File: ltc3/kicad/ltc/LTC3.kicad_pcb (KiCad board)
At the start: 4 copper layers, 175 x 150 mm, 158 parts, among them IC601 TLP3542, IC701 TLP3542, IC702 TLP3542, IC703 TLP3542, IC704 TLP3542, IC801 TLP3542, IC802 TLP3542, IC803 TLP3542, IC804 TLP3542, J601 RJ45, K601 RELAY_1C, K602 RELAY_1C, P401 43045-1000, P501 BeagleBone_Black_Expansion_He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, P502 BeagleBone_Black_Expansion_He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, P601 BATT-IN, P603 UMBILICAL, P605 43045-0200, P606 S4B-PH-K, P607 43045-0200, P608 43025-0200, P701 43045-1000, P703 43045-0800, P705 43045-0800, P801 43045-1000, P803 43045-0800, P805 43045-0800, Q401 BSS138, Q402 BSS138, Q403 BSS138, Q601 PMV45EN, Q602 PMV45EN, Q603 ZVN4525E6, Q604 ZVN4525E6, Q605 ZVN4525E6, Q701 PMV45EN, Q702 PMV45EN, Q703 PMV45EN, Q704 PMV45EN, Q801 PMV45EN, Q802 PMV45EN, Q803 PMV45EN, Q804 PMV45EN, U401 PTN78020W, U402 LTC2991, U403 PTN78020H, U404 PTN78020H, U501 24C256, U601 CD74HC14, U602 SN65220DBV, U603 741G08

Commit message: LTC3: Continued on ignition board layout
Got a solid chunk of work done on the ignition board layout.
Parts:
- moved P606 288.9 mm to (58.0, 113.0), turned to 270 degrees
- moved Q603 287.2 mm to (68.6, 113.7)
- moved R617 284.1 mm to (68.6, 118.2), turned to 270 degrees
- moved Q604 280.3 mm to (77.5, 113.7)
- moved Q605 273.8 mm to (86.3, 113.7)
- moved C602 273.4 mm to (84.1, 83.3), turned to 270 degrees
- moved K601 271.9 mm to (78.8, 97.8), turned to 180 degrees
- moved R609 270.5 mm to (93.5, 73.9), turned to 180 degrees
- moved R618 248.7 mm to (77.5, 118.2), turned to 270 degrees
- moved R619 245.9 mm to (86.3, 118.2), turned to 270 degrees
- moved K602 231.8 mm to (105.2, 95.0)
- moved P605 227.8 mm to (95.3, 114.0), turned to 0 degrees
- moved R610 220.6 mm to (99.9, 73.2), turned to 270 degrees
- moved D603 220.5 mm to (104.2, 68.7), turned to 180 degrees
- moved D605 217.7 mm to (121.5, 105.6), turned to 270 degrees
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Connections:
- net /BeagleBone Black Cape/12V_ENn renamed /12V_ENn
- net /BeagleBone Black Cape/19V_ENn renamed /19V_ENn
- net /BeagleBone Black Cape/BQ_EEPROM renamed /IGN_RTL
- net /BeagleBone Black Cape/EXT_PWR_EN_4 renamed /UMB_CONn
- net /BeagleBone Black Cape/EXT_TRG_EN_1 renamed /EXT_TRG_EN_1
- net /BeagleBone Black Cape/EXT_TRG_EN_2 renamed /EXT_TRG_EN_2
- net /BeagleBone Black Cape/EXT_TRG_EN_3 renamed /EXT_TRG_EN_3
- net /BeagleBone Black Cape/EXT_TRG_EN_4 renamed /EXT_TRG_EN_4
- net /BeagleBone Black Cape/I2C_CLOCK renamed /I2C_CLOCK
- net /BeagleBone Black Cape/I2C_DATA renamed /I2C_DATA
- net /BeagleBone Black Cape/ROCKET_READYn renamed /ROCKET_READYn
- net /External Device Power/EXT_PWR_EN_1 renamed /GPIO_EXT_PWR_1
- net /External Device Power/EXT_PWR_EN_2 renamed /GPIO_EXT_PWR_2
- net /External Device Power/EXT_PWR_EN_3 renamed /GPIO_EXT_PWR_3
- net /External Device Power/EXT_PWR_EN_4 renamed /GPIO_EXT_PWR_4
- K601 pad 1: (no net) -> /Rocket Umbilical & Ignition Control/IGN_BATT_P
- K601 pad 2: (no net) -> +5V
- K601 pad 3: (no net) -> Net-(K601-Pad3)
- K601 pad 5: (no net) -> Net-(D601-Pad2)
- K602 pad 1: (no net) -> Net-(K601-Pad3)
- K602 pad 2: (no net) -> +5V
- K602 pad 3: (no net) -> Net-(K602-Pad3)
- K602 pad 5: (no net) -> Net-(D604-Pad2)
- P605 pad 1: Net-(K602-Pad87) -> Net-(K602-Pad3)
- Q603 pad 3: Net-(K601-Pad87) -> Net-(K601-Pad3)
- Q604 pad 3: Net-(K602-Pad87) -> Net-(K602-Pad3)
- R617 pad 1: Net-(K601-Pad87) -> Net-(K601-Pad3)
- R618 pad 1: Net-(K602-Pad87) -> Net-(K602-Pad3)
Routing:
- net +5V: track 11.8 -> 124.4 mm
- net Net-(K602-Pad3): track 0.00 -> 63.6 mm
- net Net-(K601-Pad3): track 0.00 -> 52.7 mm
- net Net-(P606-Pad3): track 0.00 -> 39.8 mm
- net Net-(P606-Pad2): track 0.00 -> 33.6 mm
- net Net-(P605-Pad2): track 0.00 -> 32.5 mm
- net /Rocket Umbilical & Ignition Control/IGN_BATT_P: track 0.00 -> 31.1 mm
- net /Rocket Umbilical & Ignition Control/UMB_CONN_FROM_RKT: track 0.00 -> 25.3 mm
- net Net-(C601-Pad1): track 0.00 -> 22.9 mm
- net Net-(R610-Pad1): track 0.00 -> 21.5 mm, vias 0 -> 2
- net Net-(D601-Pad2): track 0.00 -> 21.3 mm
- net Net-(D602-Pad1): track 0.00 -> 20.8 mm, vias 0 -> 2
- net Net-(R605-Pad1): track 0.00 -> 19.8 mm
- net /Rocket Umbilical & Ignition Control/ROCKET_READY_5V: track 0.00 -> 17.5 mm
- net Net-(IC601-Pad6): track 0.00 -> 17.0 mm
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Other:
- board outline removed
- board text added: "READY FOR LAUNCH"

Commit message: LTC3: Main Board Layout con't
For the most part finished a layout of the main LTC3 board!  Hooray!
Had to adjust a symbol and hoping that it doesn't mess up the library.

Todo: Figure out of this is 4 layer or 2 layer board.  May be doable as 2.
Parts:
- moved P608 441.2 mm to (-99.1, 112.8)
- moved R803 250.2 mm to (106.2, 154.4), turned to 0 degrees
- moved Q801 242.7 mm to (106.2, 150.9)
- moved R804 239.3 mm to (124.5, 154.4), turned to 0 degrees
- moved R801 236.5 mm to (113.8, 140.7)
- moved IC801 235.4 mm to (109.7, 139.7), turned to 180 degrees
- moved R807 231.9 mm to (142.7, 154.4), turned to 0 degrees
- moved R802 225.7 mm to (132.1, 140.7)
- moved JP801 225.5 mm to (126.0, 117.3), turned to 0 degrees
- moved P801 222.0 mm to (117.0, 179.1), turned to 0 degrees
- moved Q802 220.9 mm to (124.5, 150.9)
- moved C606 220.7 mm to (155.2, 68.8), turned to 270 degrees
- moved W605 220.0 mm to (163.1, 61.0), turned to 90 degrees
- moved P803 219.1 mm to (138.2, 179.1), turned to 0 degrees
- moved R808 217.2 mm to (162.1, 154.4), turned to 0 degrees
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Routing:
- net Net-(JP801-Pad2): track 0.00 -> 120.2 mm, vias 0 -> 2
- net Net-(IC802-Pad4): track 0.00 -> 116.9 mm, vias 0 -> 2
- net /External Device Triggers/EXT_TRG_4_LED_CATH: track 0.00 -> 114.1 mm, vias 0 -> 2
- net Net-(IC801-Pad4): track 0.00 -> 106.4 mm, vias 0 -> 2
- net /External Device Triggers/EXT_TRG_1_LED_CATH: track 0.00 -> 85.2 mm
- net /External Device Triggers/EXT_TRG_3_LED_CATH: track 0.00 -> 82.7 mm, vias 0 -> 2
- net +5V: track 124.4 -> 201.1 mm
- net /External Device Triggers/EXT_TRG_4_OPTO_RELAY: track 0.00 -> 74.2 mm, vias 0 -> 2
- net Net-(JP802-Pad2): track 0.00 -> 72.5 mm, vias 0 -> 2
- net Net-(JP804-Pad2): track 0.00 -> 71.6 mm, vias 0 -> 2
- net /External Device Triggers/EXT_TRG_1_FET_D: track 0.00 -> 70.3 mm
- net Net-(JP803-Pad2): track 0.00 -> 65.7 mm, vias 0 -> 2
- net /External Device Triggers/EXT_TRG_4_FET_D: track 0.00 -> 64.0 mm
- net /External Device Triggers/EXT_TRG_2_FET_D: track 0.00 -> 63.7 mm
- net /External Device Triggers/EXT_TRG_1_OPTO_RELAY: track 0.00 -> 59.5 mm, vias 0 -> 2
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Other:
- board outline added: 202.2 x 150.4 mm

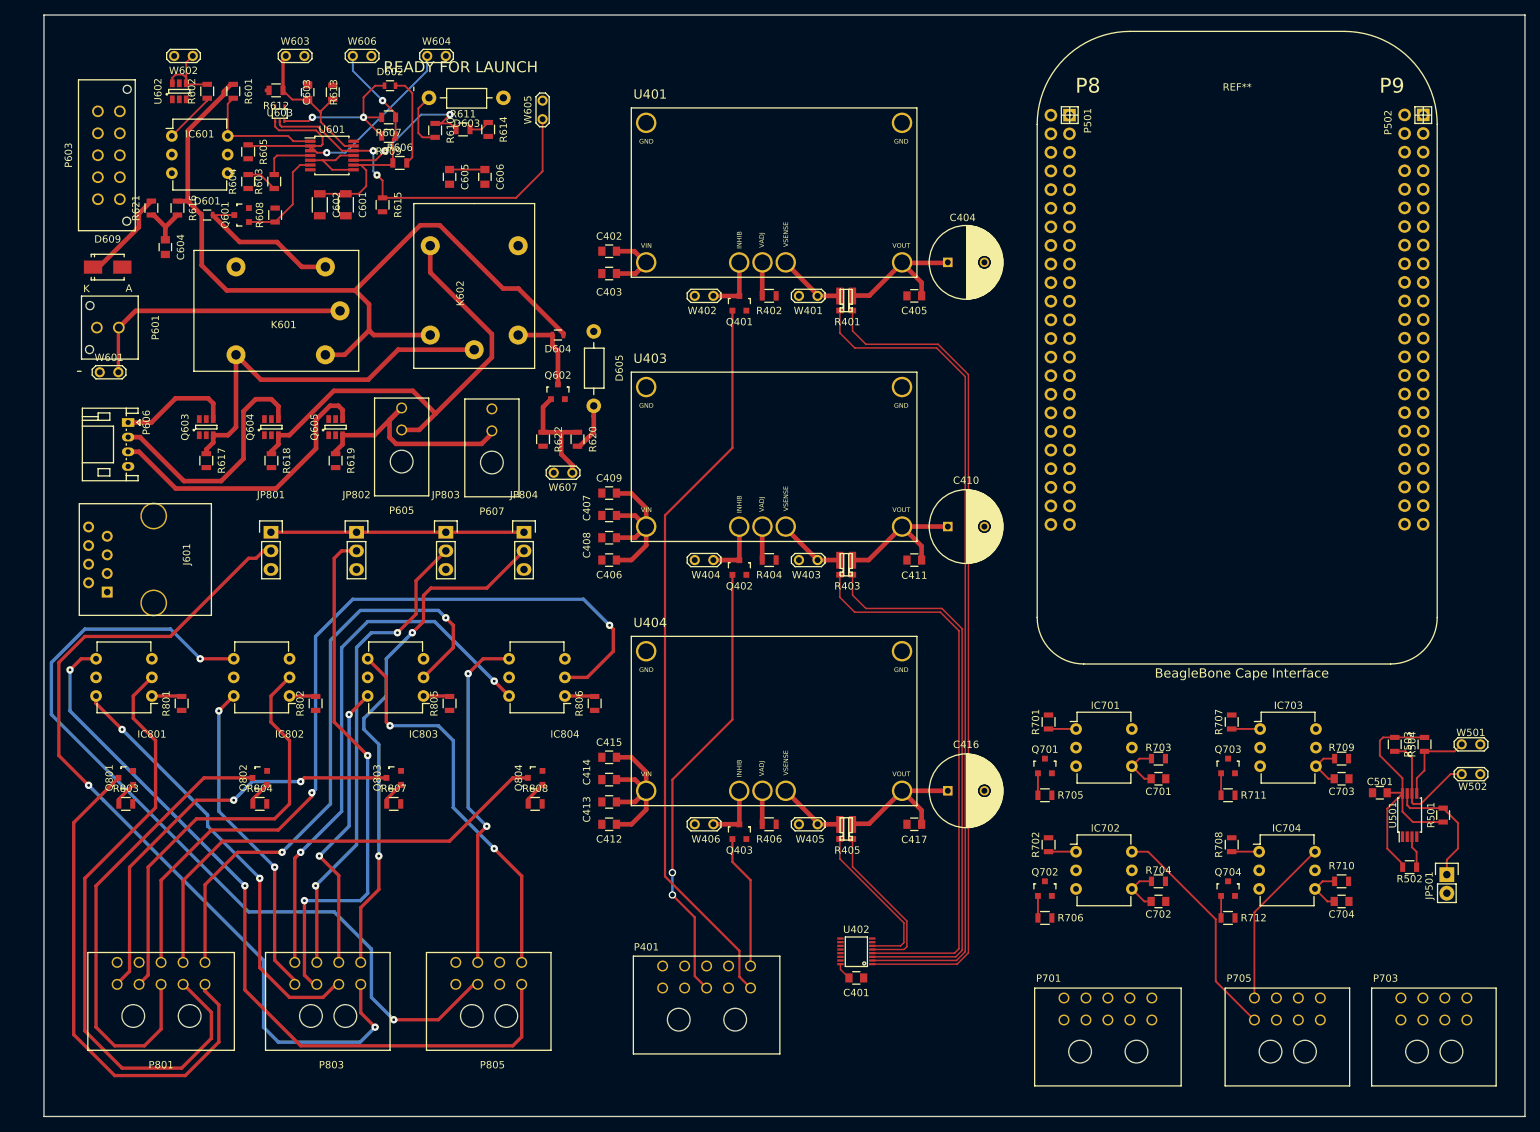
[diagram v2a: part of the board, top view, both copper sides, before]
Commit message: LTC3: More LTC layout work
Came to a rough finale of the LTC board layout.
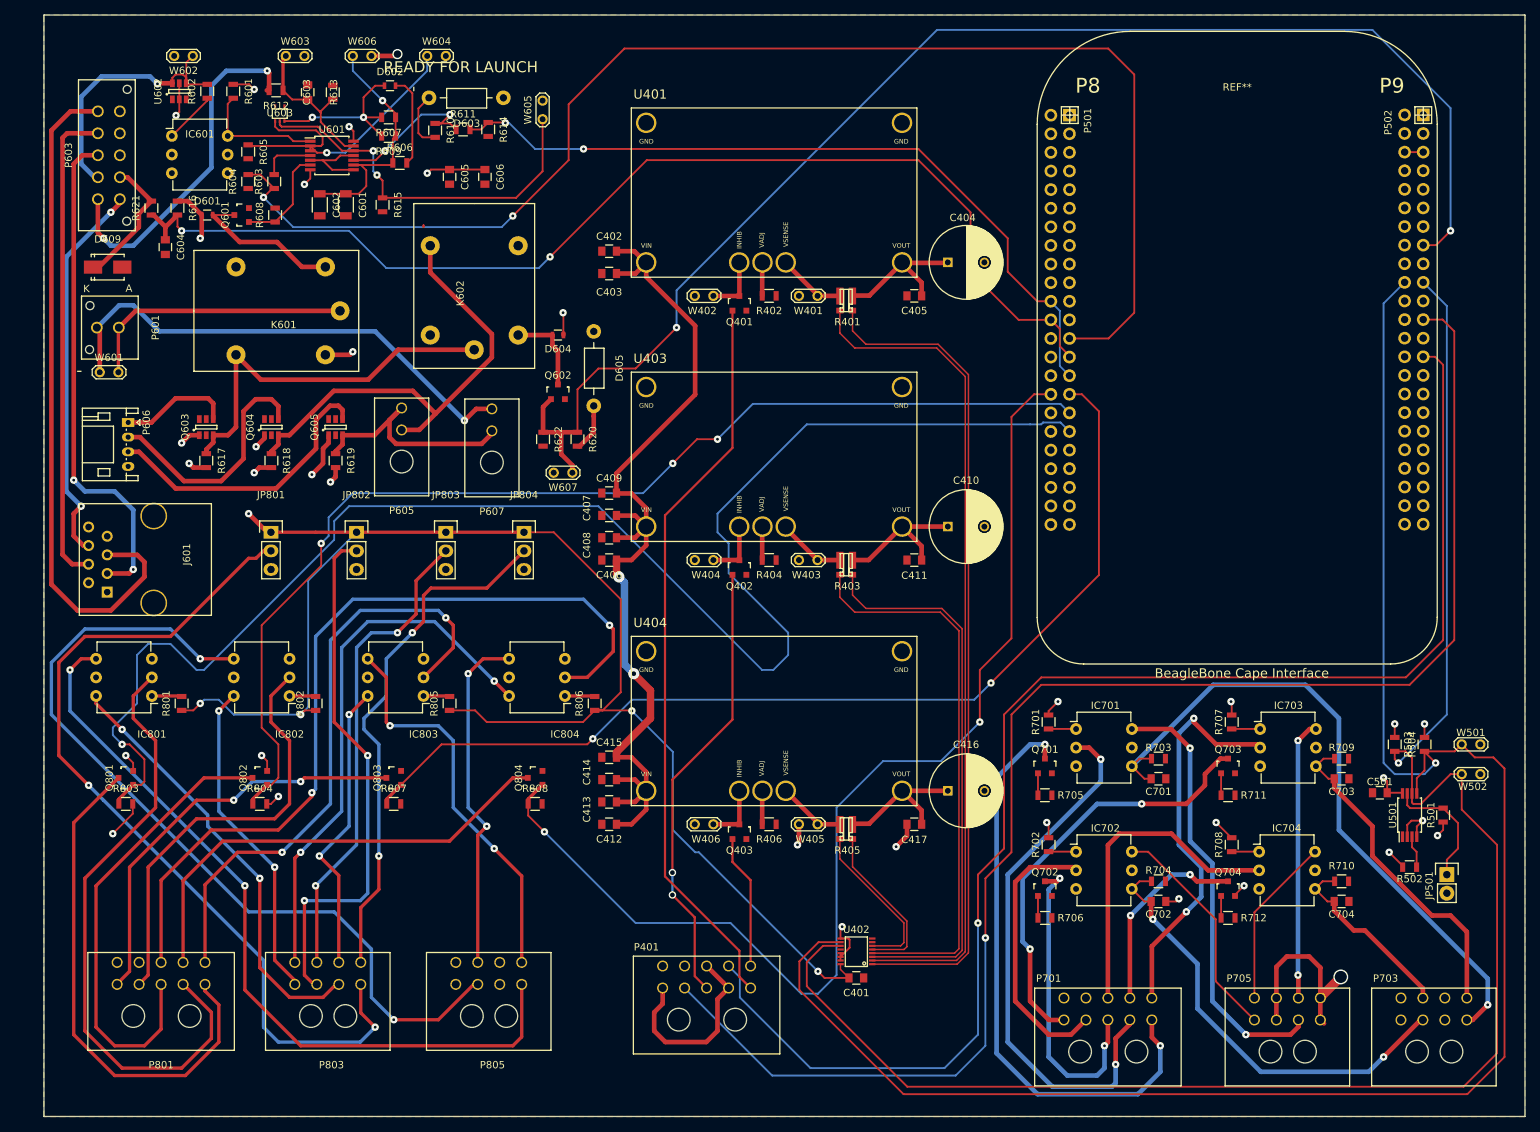
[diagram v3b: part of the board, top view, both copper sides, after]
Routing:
- net +19V: track 9.75 -> 281.7 mm, vias 0 -> 2
- net /I2C_DATA: track 11.7 -> 250.5 mm, vias 0 -> 1
- net /I2C_CLOCK: track 17.4 -> 239.6 mm, vias 0 -> 1
- net /EXT_TRG_EN_1: track 3.41 -> 215.0 mm, vias 0 -> 1
- net /12V_ENn: track 0.00 -> 206.1 mm, vias 0 -> 1
- net /19V_ENn: track 0.00 -> 193.4 mm, vias 0 -> 1
- net /ROCKET_READYn: track 4.34 -> 185.7 mm, vias 0 -> 2
- net /BeagleBone Black Cape/ROCKET_IGNITE: track 15.8 -> 189.9 mm, vias 0 -> 2
- net /EXT_TRG_EN_4: track 3.41 -> 155.6 mm, vias 0 -> 2
- net /EXT_TRG_EN_2: track 3.41 -> 153.7 mm, vias 0 -> 3
- net /UMB_CONn: track 6.68 -> 155.9 mm, vias 0 -> 2
- net /EXT_TRG_EN_3: track 3.41 -> 137.9 mm, vias 0 -> 2
- net /IGN_RTL: track 2.87 -> 103.7 mm, vias 0 -> 2
- net /Rocket Umbilical & Ignition Control/ROCKET_ETH_3: track 0.00 -> 93.0 mm
- net Net-(C701-Pad1): track 6.45 -> 92.5 mm, vias 0 -> 1
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- added copper zone on Power.Cu, net +12V
- added copper zone on Power.Cu, net +5V
- added copper zone on F.Cu, net GND
- added copper zone on Ground.Cu, net GND

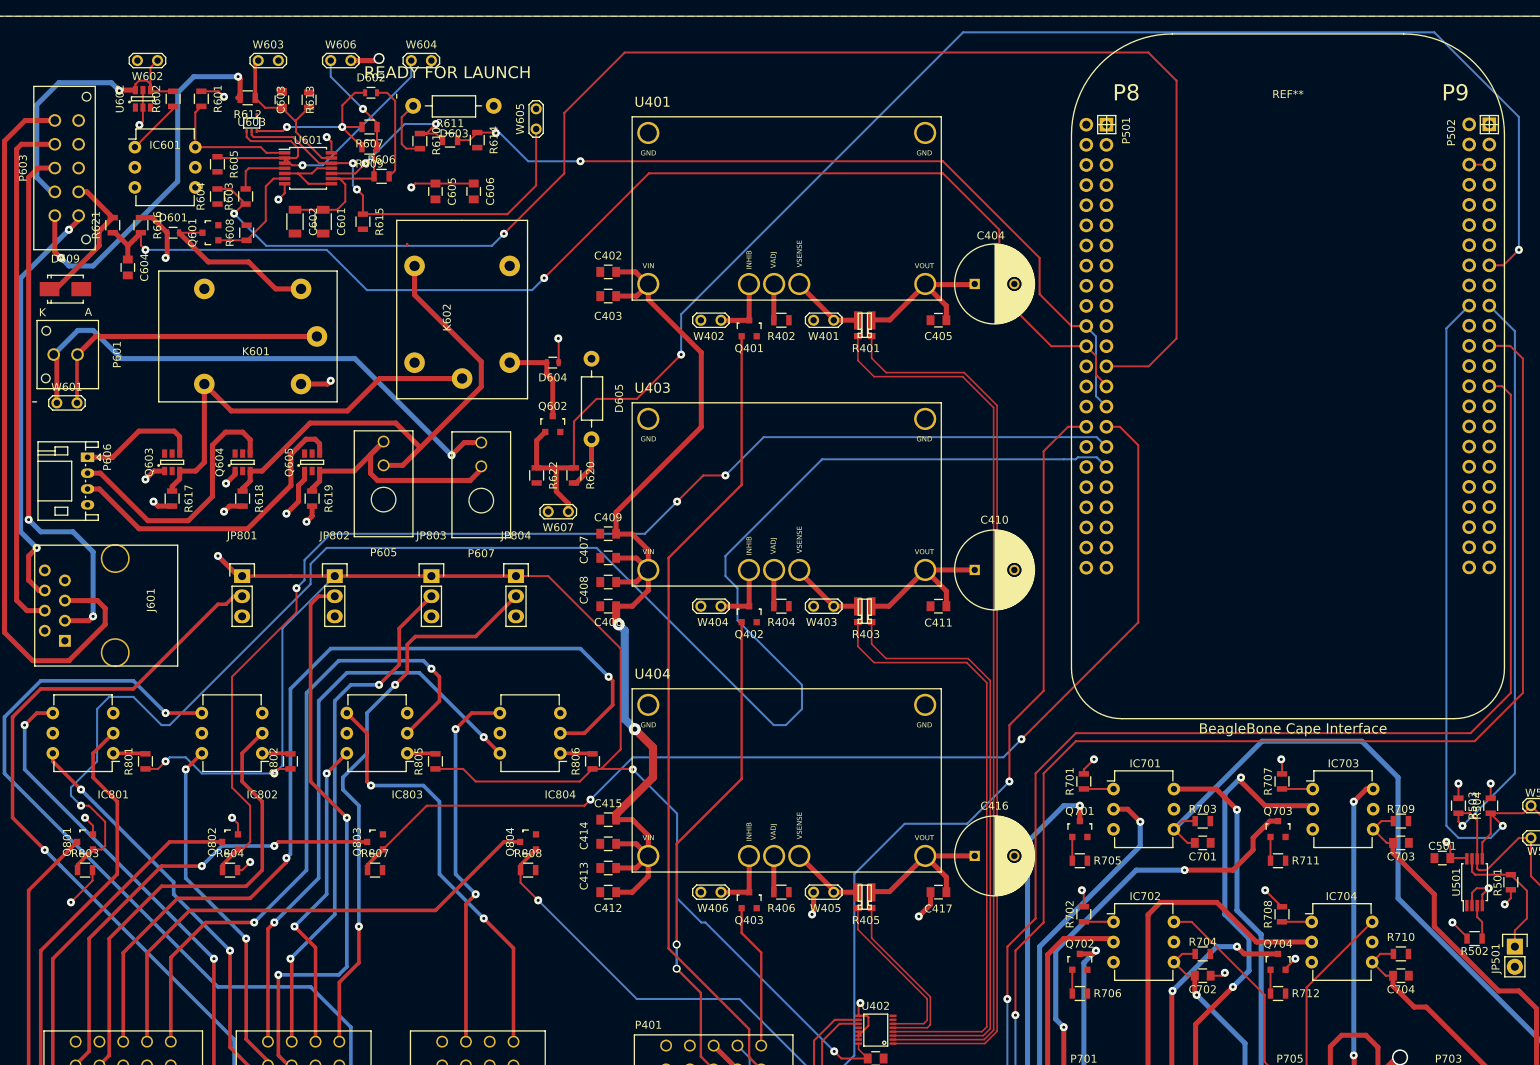
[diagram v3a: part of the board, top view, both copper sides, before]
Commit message: LTC3: Layout
Moved silk screen references so they are visible.
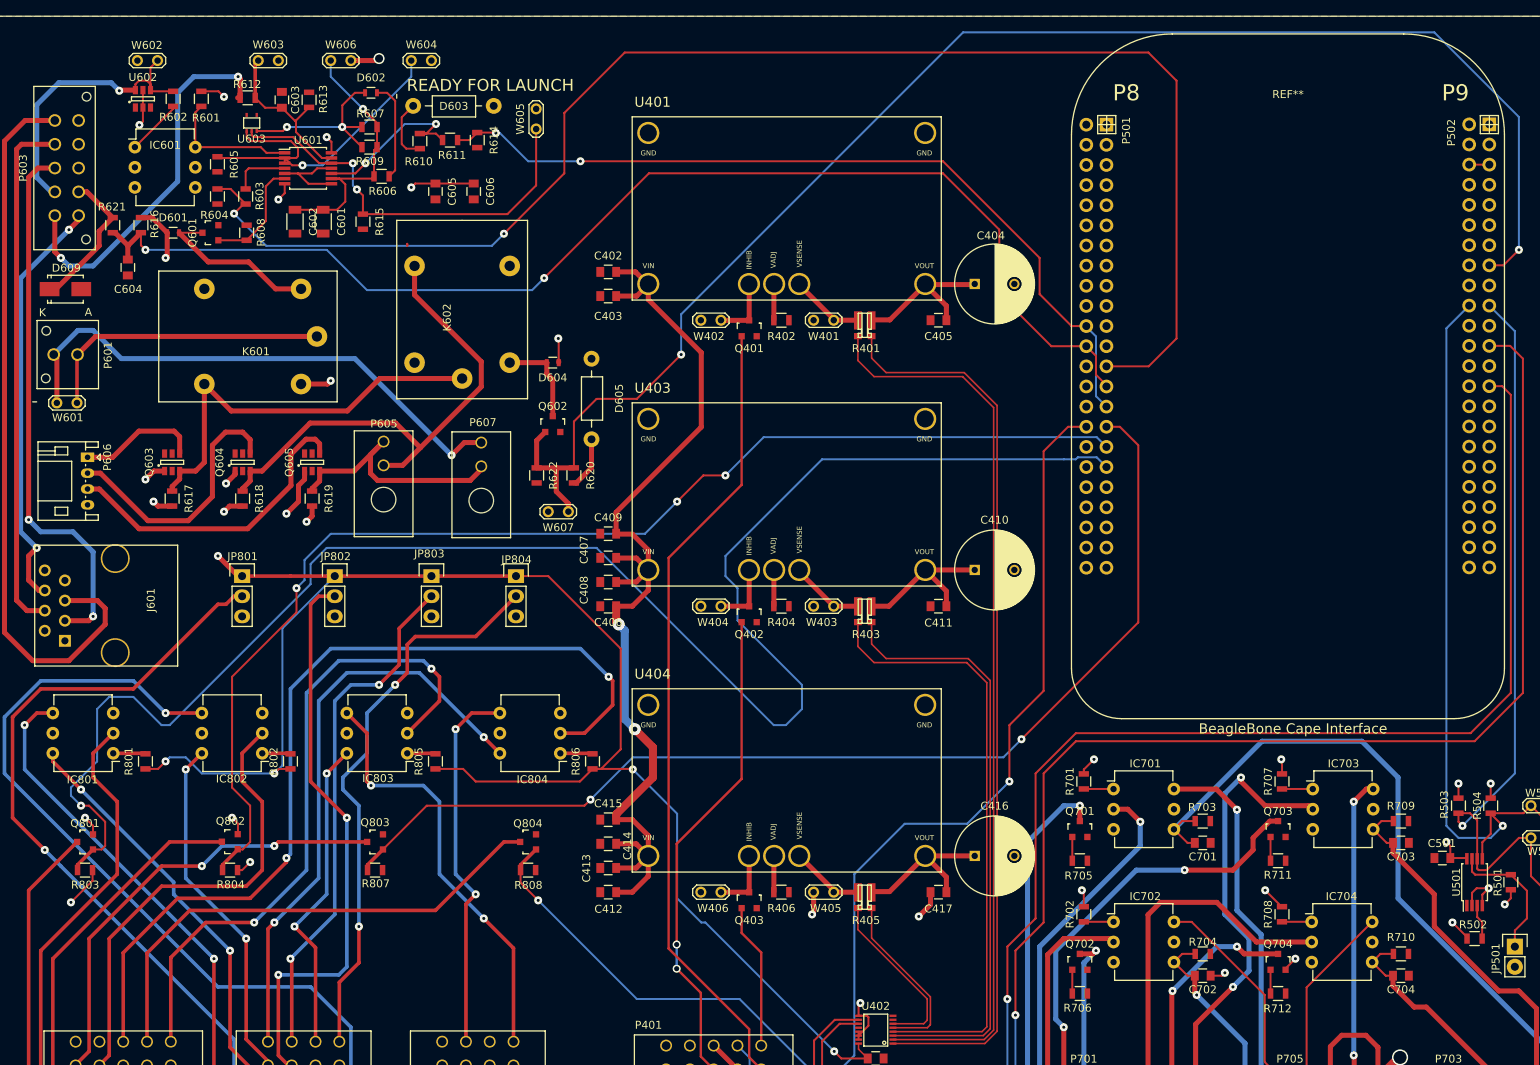
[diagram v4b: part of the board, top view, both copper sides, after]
